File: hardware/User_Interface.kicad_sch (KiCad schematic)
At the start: 0 parts

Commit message: Added connectors to display schematic
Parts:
- added C18: 100nF, symbol Device:C
- added C31, C32: 1uF, symbol Device:C
- added J2: AYF531035, symbol Connector_Generic:Conn_01x10
- added J3: Molex 5034800440, symbol Connector_Generic:Conn_01x04
- added R3, R9: 0, symbol Device:R_US
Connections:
- new net +3V3: C18.1, C31.1, C32.1, J2.5 (Pin_5), J2.6 (Pin_6), J2.7 (Pin_7), R3.1
- new net EXTMODE: J2.8 (Pin_8), R3.2, R9.1
- new net GND: C18.2, C31.2, C32.2, J2.10 (Pin_10), J2.9 (Pin_9), R9.2
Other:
- note added: "Backlight Power"
- note added: "Communication"
- note added: "The display used is the Sharp LS013B7DH03 This display is "memory in pixel", meaning that the image on the LCD could be static for long periods of time. To prevent image burning on the LCD the common electrode (COM) needs to be periodically flipped. Flipping the common electrode can be done in 2 different ways: 1. When you send a SPI command, you can tell the display to flip the COM. This would m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"

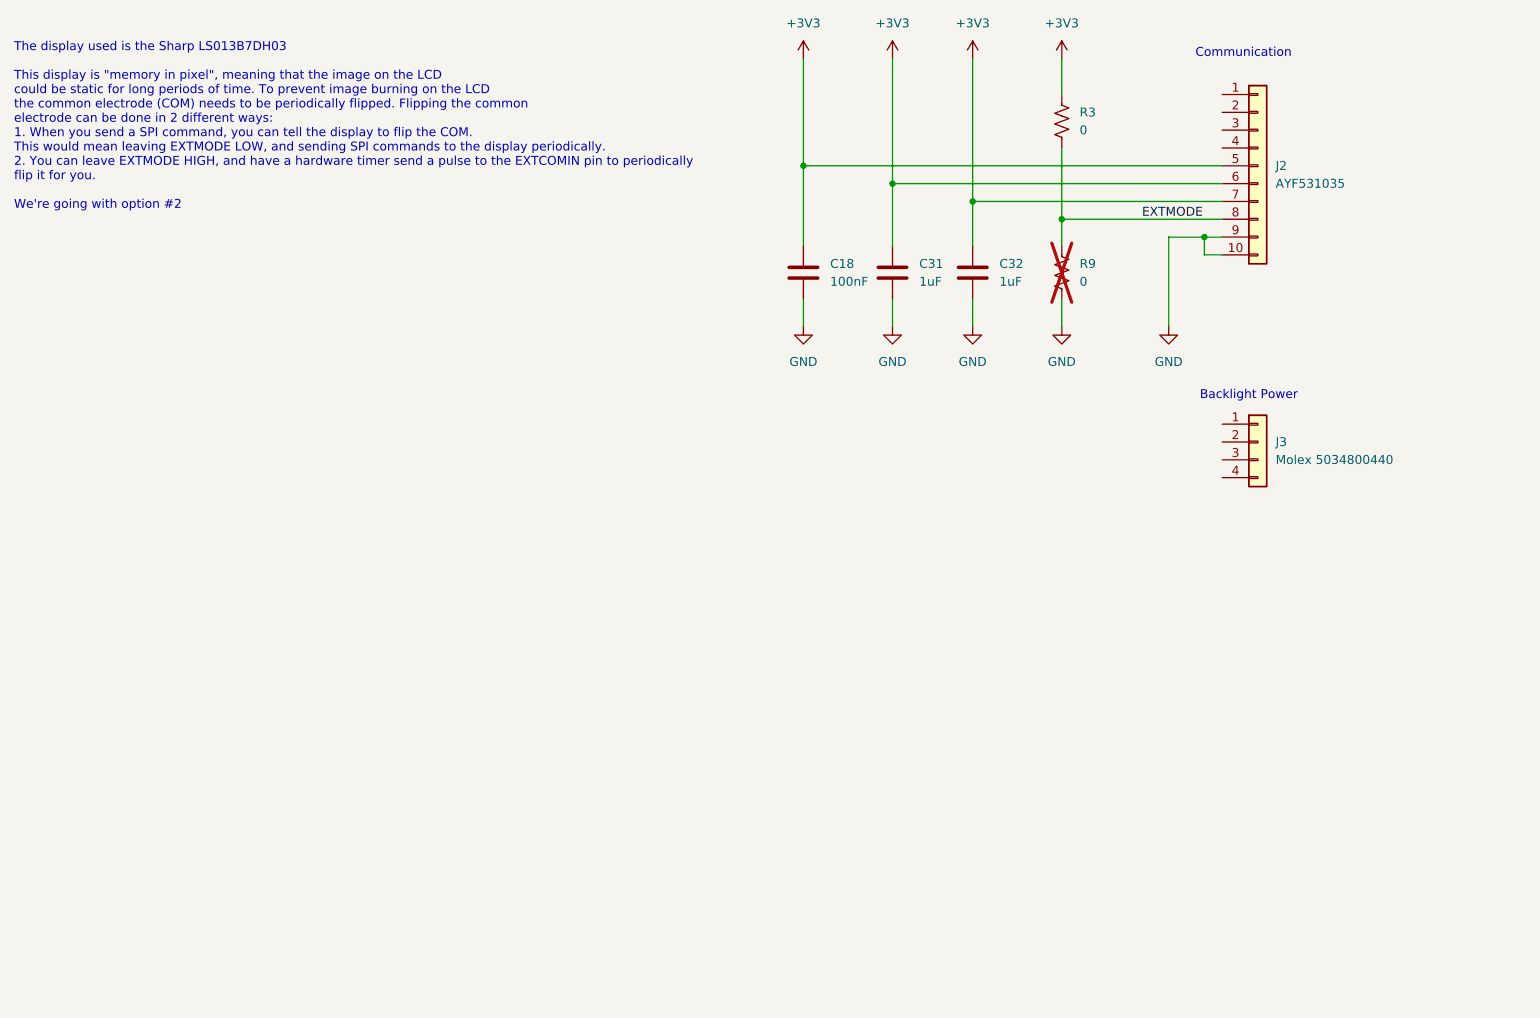
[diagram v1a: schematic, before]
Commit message: Completed display schematic
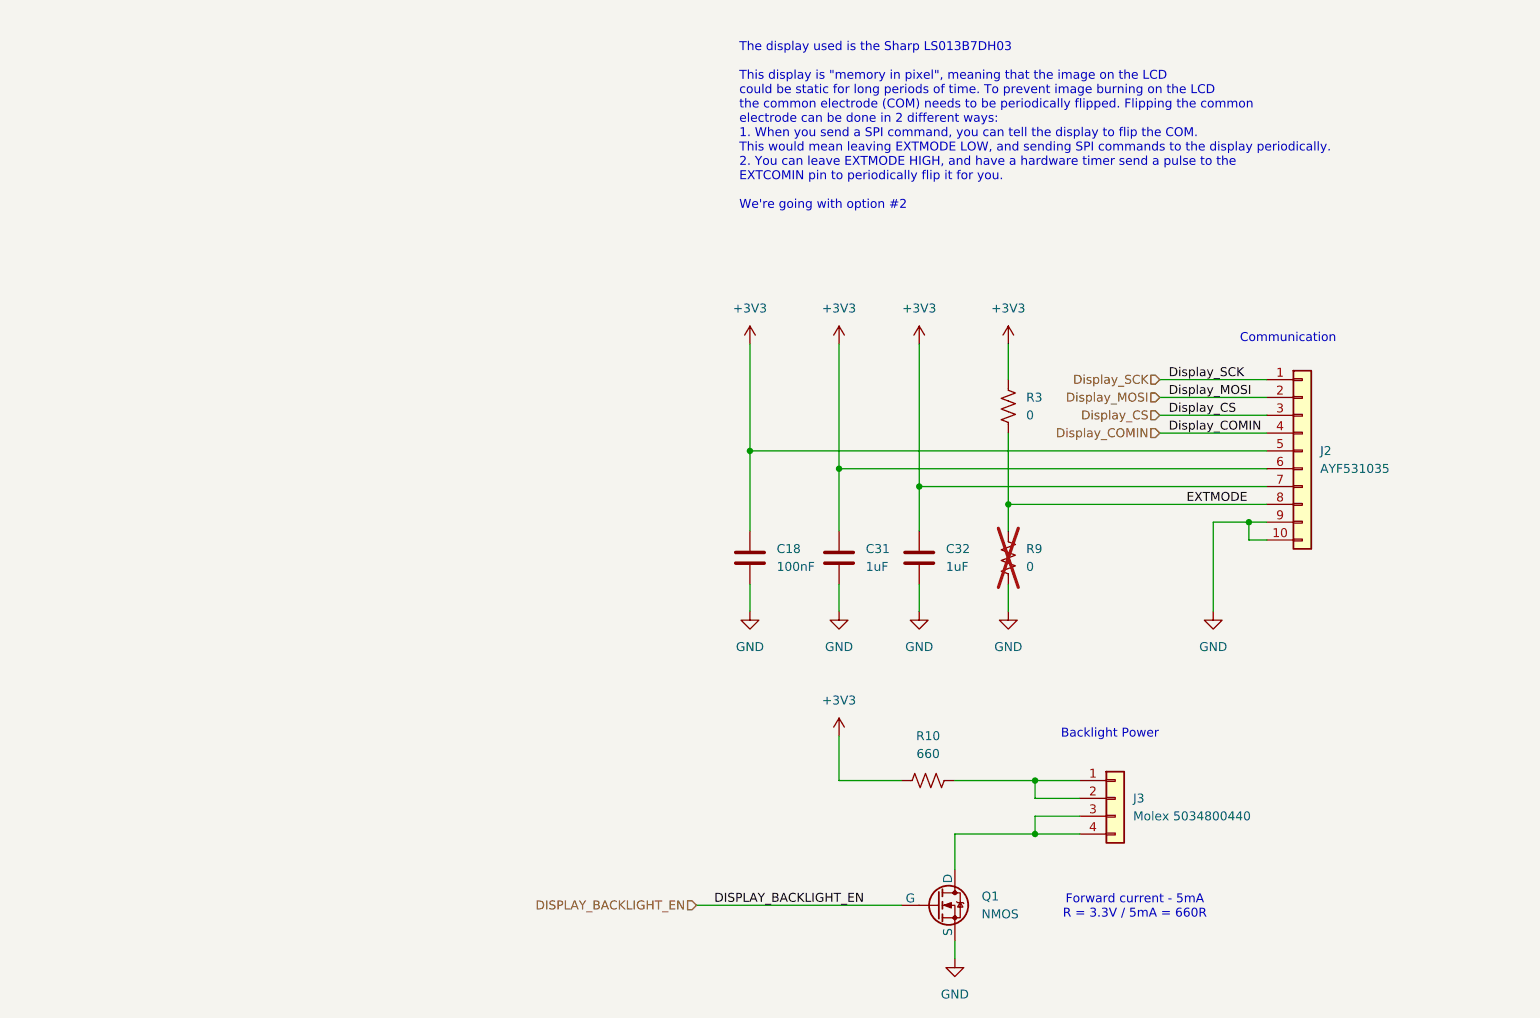
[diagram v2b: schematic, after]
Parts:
- added Q1: NMOS, symbol Simulation_SPICE:NMOS
- added R10: 660, symbol Device:R_US
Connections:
- net +3V3: now also R10.1
- net GND: now also Q1.3 (S)
- net Display_SCK: now reaches J2.1 (Pin_1)
- net Display_MOSI: now reaches J2.2 (Pin_2)
- net Display_CS: now reaches J2.3 (Pin_3)
- net Display_COMIN: now reaches J2.4 (Pin_4)
- net at J3.1 (Pin_1): now also J3.2 (Pin_2), R10.2
- net at J3.3 (Pin_3): now also J3.4 (Pin_4), Q1.1 (D)
- new net DISPLAY_BACKLIGHT_EN: Q1.2 (G)
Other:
- note added: "Forward current - 5mA R = 3.3V / 5mA = 660R"
- moved on the sheet: C18, C31, C32, J2, J3, R3, R9

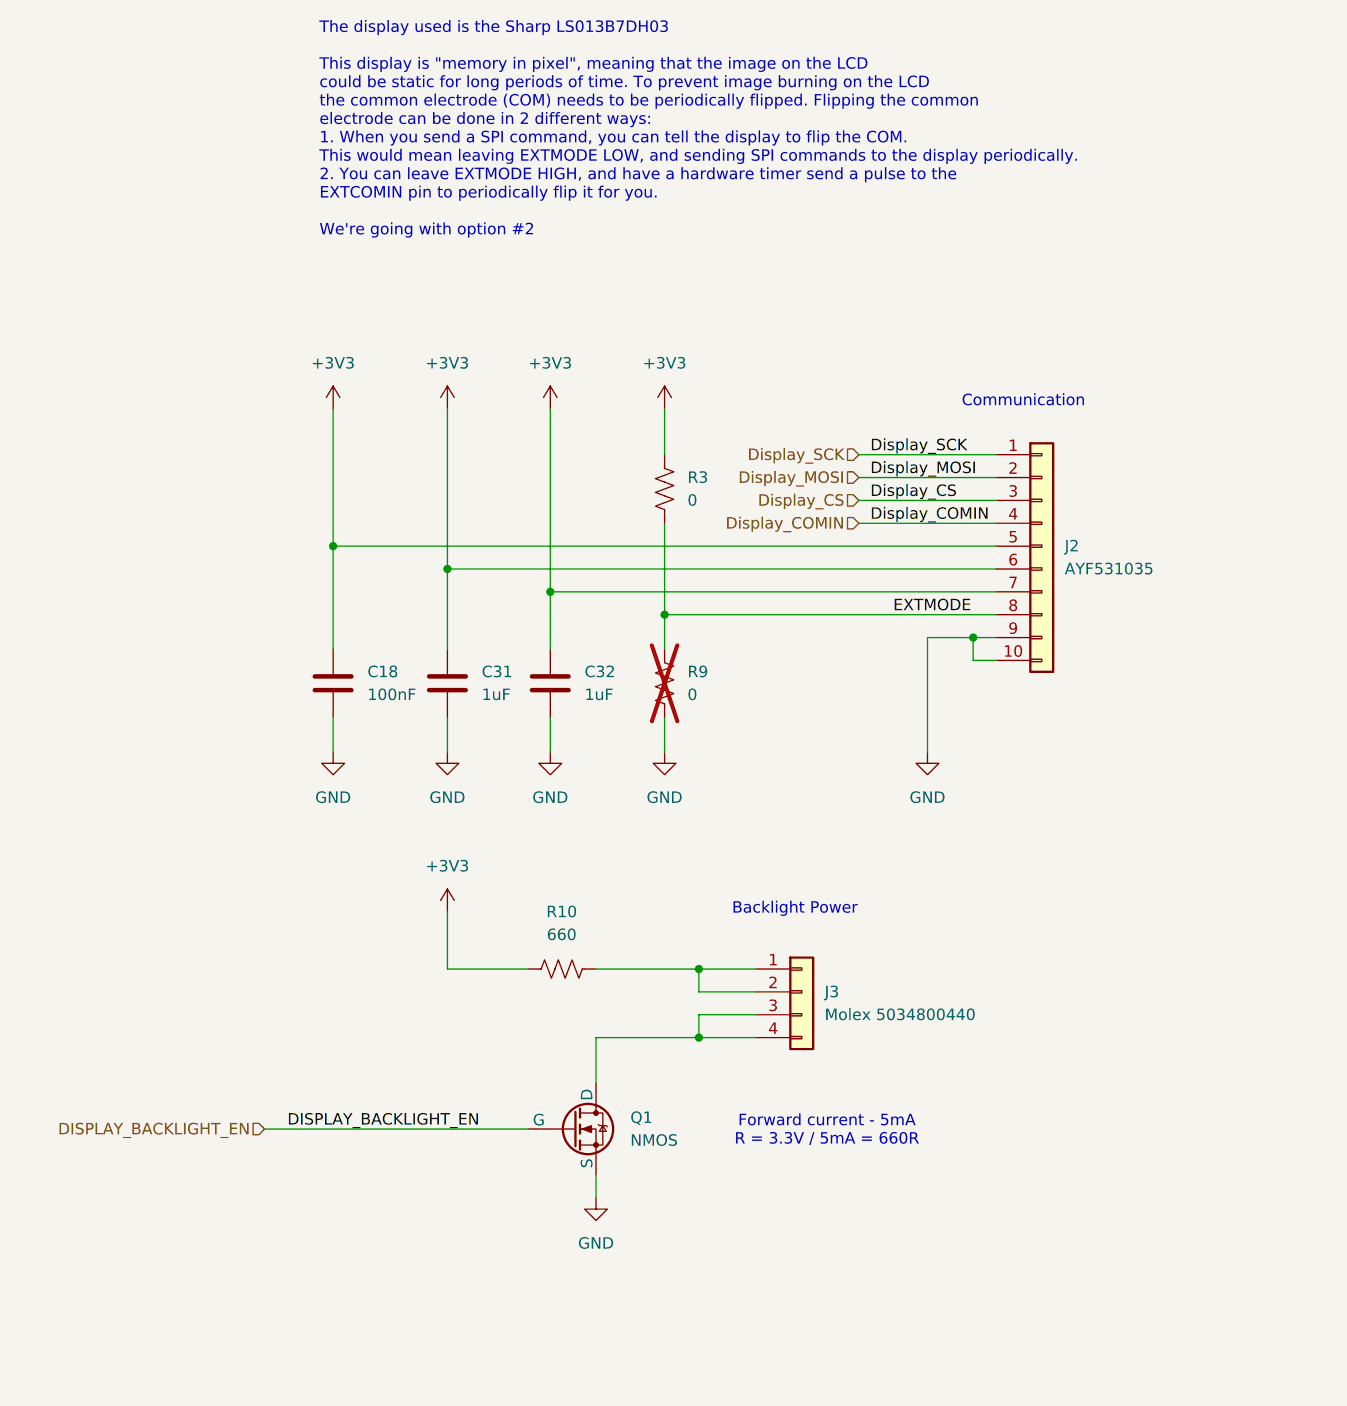
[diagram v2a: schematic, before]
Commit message: Added bluetooth module schematic and environmental perception block"
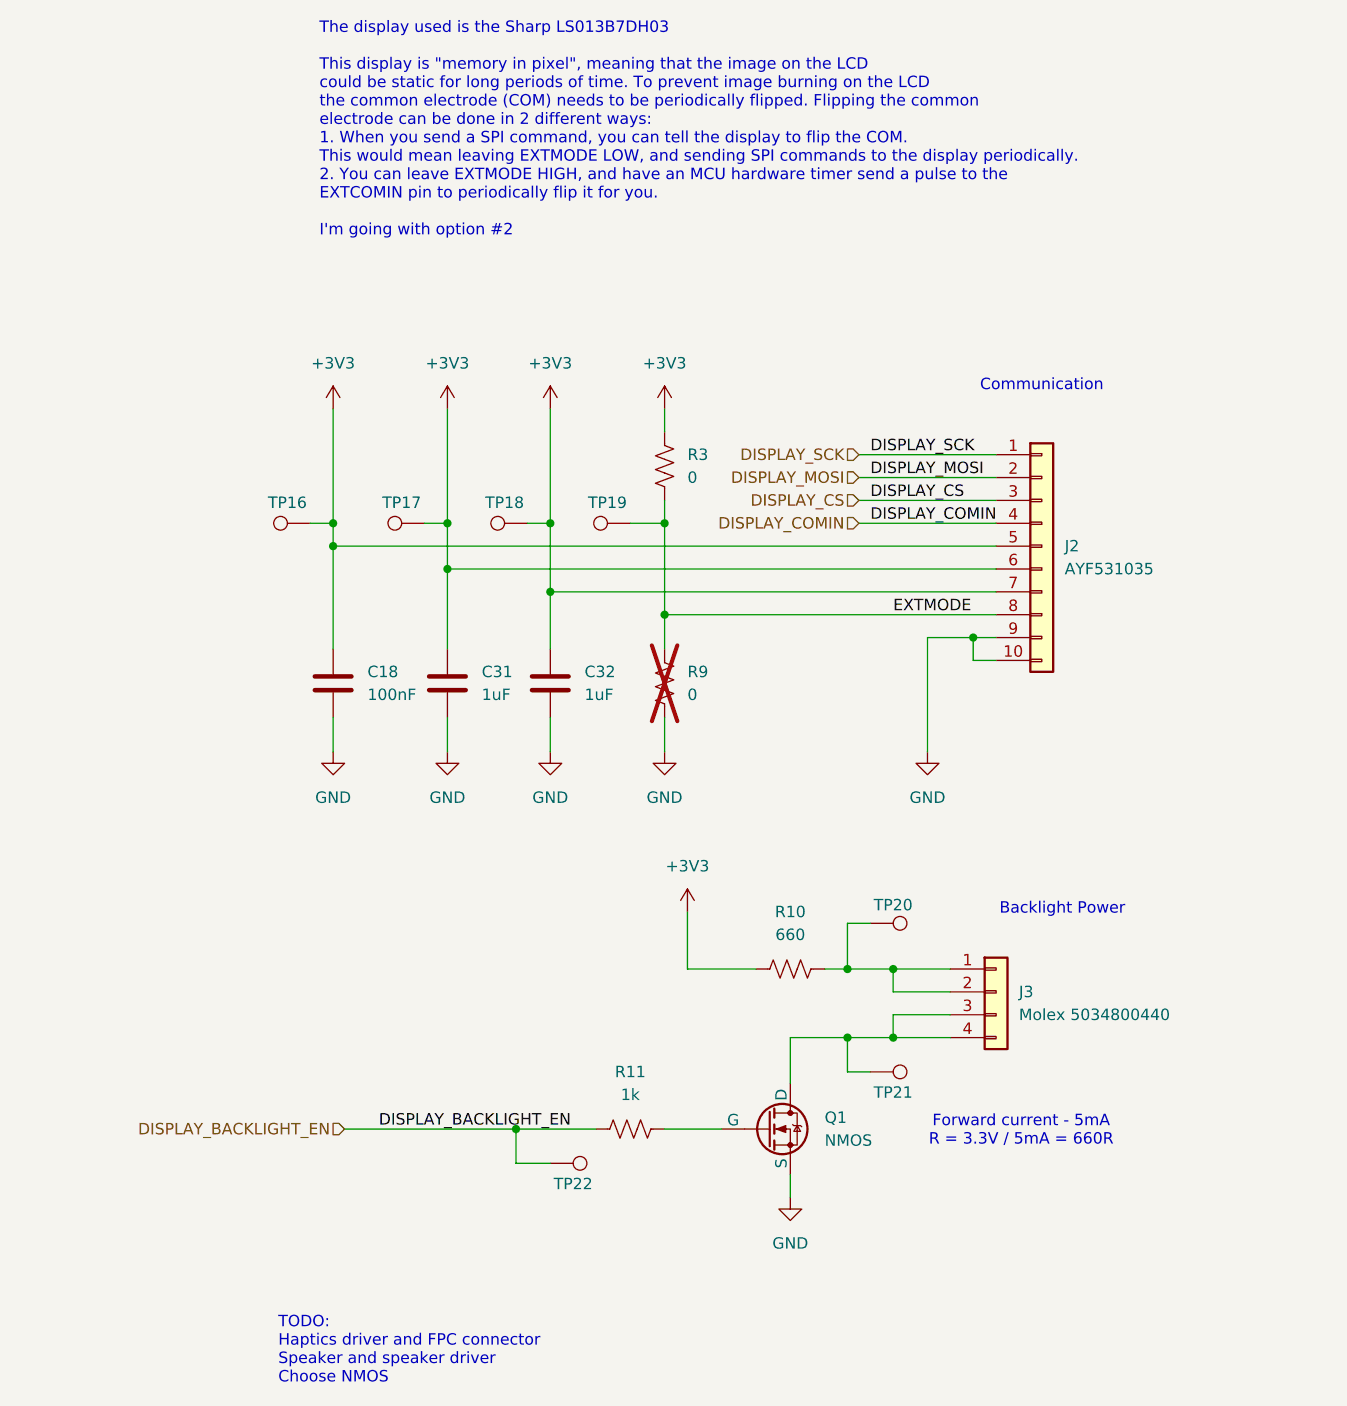
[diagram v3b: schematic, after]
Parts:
- added R11: 1k, symbol Device:R_US
- added TP16, TP17, TP18, TP19, TP20, TP21, TP22: TestPoint, symbol Connector:TestPoint
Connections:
- net +3V3: now also TP16.1, TP17.1, TP18.1
- net DISPLAY_BACKLIGHT_EN: now also R11.1, TP22.1; no longer Q1.2 (G)
- net EXTMODE: now also TP19.1
- net at J3.3 (Pin_3), J3.4 (Pin_4), Q1.1 (D): now also TP21.1
- net at J3.1 (Pin_1), J3.2 (Pin_2), R10.2: now also TP20.1
- net Display_COMIN renamed DISPLAY_COMIN
- net Display_CS renamed DISPLAY_CS
- net Display_MOSI renamed DISPLAY_MOSI
- net Display_SCK renamed DISPLAY_SCK
- new net: Q1.2 (G), R11.2
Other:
- note added: "TODO: Haptics driver and FPC connector Speaker and speaker driver Choose NMOS"
- moved on the sheet: J3, Q1, R10, R3

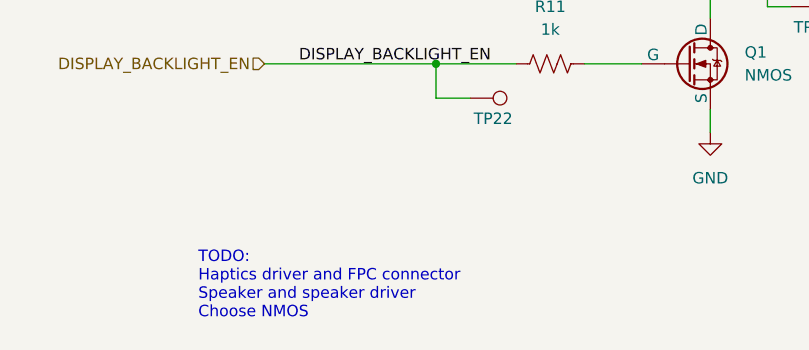
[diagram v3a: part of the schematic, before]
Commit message: Changing barometer, STM32 and power rails
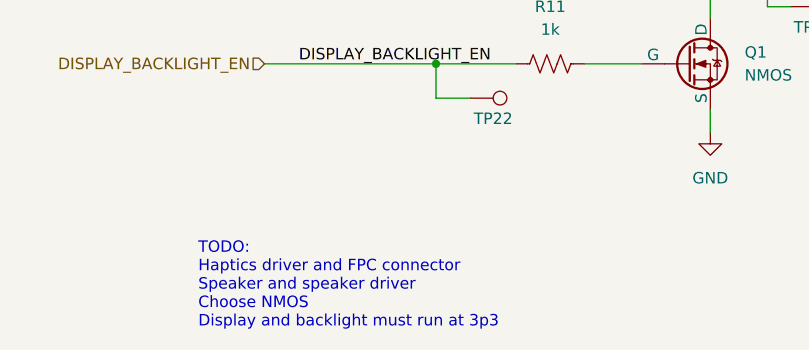
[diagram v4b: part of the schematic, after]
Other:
- note added: "TODO: Haptics driver and FPC connector Speaker and speaker driver Choose NMOS Display and backlight must run at 3p3"
- note removed: "TODO: Haptics driver and FPC connector Speaker and speaker driver Choose NMOS"
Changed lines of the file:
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@@
 		)
 	)
-	(text "TODO:\nHaptics driver and FPC connector\nSpeaker and speaker driver\nChoose NMOS"
+	(text "TODO:\nHaptics driver and FPC connector\nSpeaker and speaker driver\nChoose NMOS\nDisplay and backlight must run at 3p3"
 		(exclude_from_sim no)
 		(at 179.324 171.958 0)

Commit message: Contemplating switching back to the 64LQFP
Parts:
- added Q2: NMOS, symbol Simulation_SPICE:NMOS
- added R15: 1k, symbol Device:R_US
- added R16: 100k, symbol Device:R_US
- added TP23: TestPoint, symbol Connector:TestPoint
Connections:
- net +3V3: now also R16.2
- net DISPLAY_COMIN: now also R15.1, TP23.1; no longer J2.4 (Pin_4)
- net GND: now also Q2.3 (S)
- new net: Q2.2 (G), R15.2
- new net DISPLAY_COMIN_3P3: J2.4 (Pin_4), Q2.1 (D), R16.1
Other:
- note added: "Capacitance on this line must be less than 166nF"
